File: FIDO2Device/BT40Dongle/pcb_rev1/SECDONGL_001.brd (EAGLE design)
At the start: 24 x 34 mm, 38 parts, among them CN1 CX60-24S-UNIT, CN2 IF_5PIN_H, CN3 IF_2PIN_SOL, SW1 SKRPACE010, SW2 SKRPACE010, SW3 SKTADAE010, U1 BT40, U2 ADP122ACPZ-3.3-R7, U3 RV-3028-C7

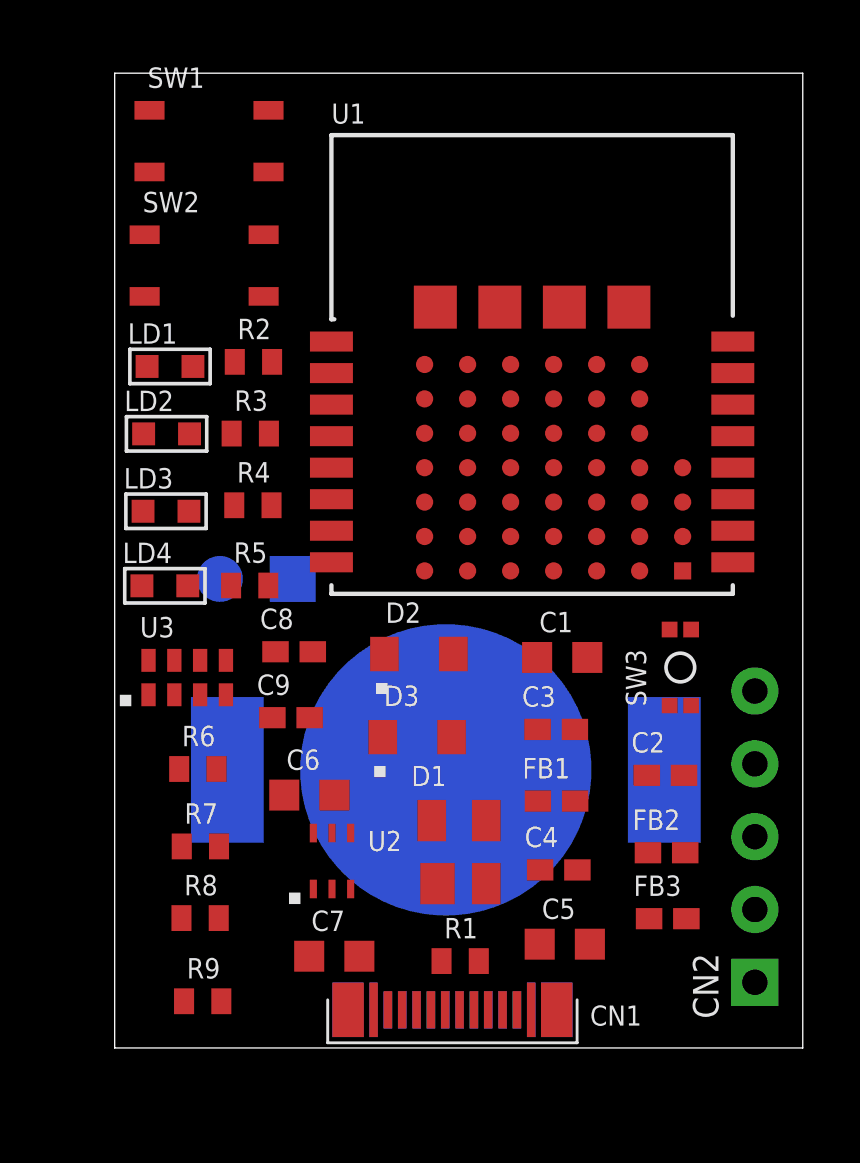
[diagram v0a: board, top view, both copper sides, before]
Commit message: 配線レイアウトを作成
・部品のおおまかなレイアウトを設定
・チップ抵抗のパッケージから、Keepoutを削除
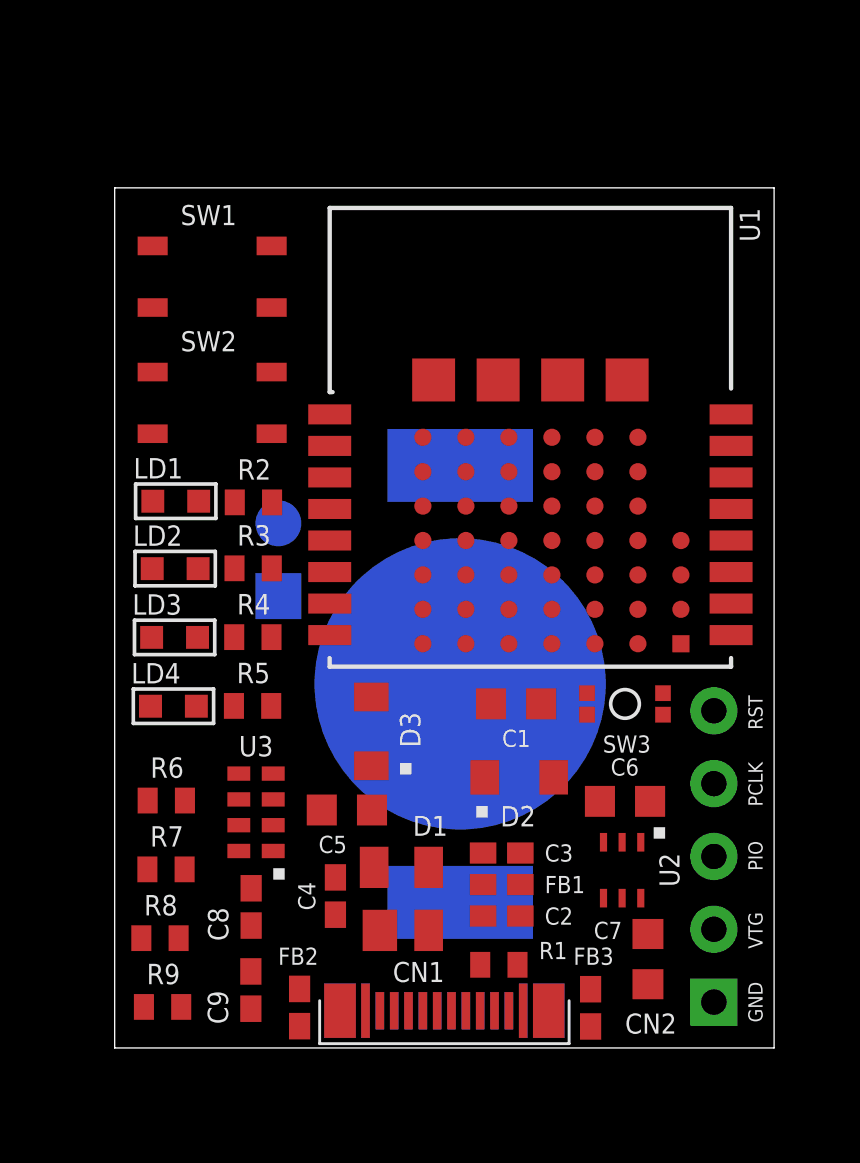
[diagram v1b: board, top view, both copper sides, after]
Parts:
- moved FB2 13.9 mm to (6.45, 1.41), turned to 270 degrees
- moved C6 11.0 mm to (17.8, 8.60), turned to 180 degrees
- moved C7 10.9 mm to (18.6, 3.10), turned to 270 degrees
- moved U2 10.1 mm to (17.7, 6.20), turned to 180 degrees
- moved C9 9.60 mm to (4.75, 2.02), turned to 90 degrees
- moved C8 9.03 mm to (4.76, 4.92), turned to 90 degrees
- moved C5 8.93 mm to (8.10, 8.30), turned to 180 degrees
- moved C4 7.84 mm to (7.70, 5.30), turned to 270 degrees
- moved C2 7.53 mm to (13.5, 4.60)
- moved U3 7.29 mm to (5.93, 6.62), turned to 90 degrees
- moved D2 5.54 mm to (14.1, 9.44)
- moved R2 4.90 mm to (4.84, 19.0)
- moved SW2 4.80 mm to (3.40, 22.5)
- moved SW1 4.73 mm to (3.40, 26.9)
- moved C3 4.71 mm to (13.5, 6.80)
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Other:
- board size 24 x 34 mm -> 23 x 30 mm
- board text added: "GND"
- board text added: "PCLK"
- board text added: "PIO"
- board text added: "RST"
- board text added: "VTG"

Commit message: 配線レイアウトの作成
・サイズを小型化（30mm x 20mm）するため、部品レイアウトを修正
・部品番号を変更（FBx --> Lx）
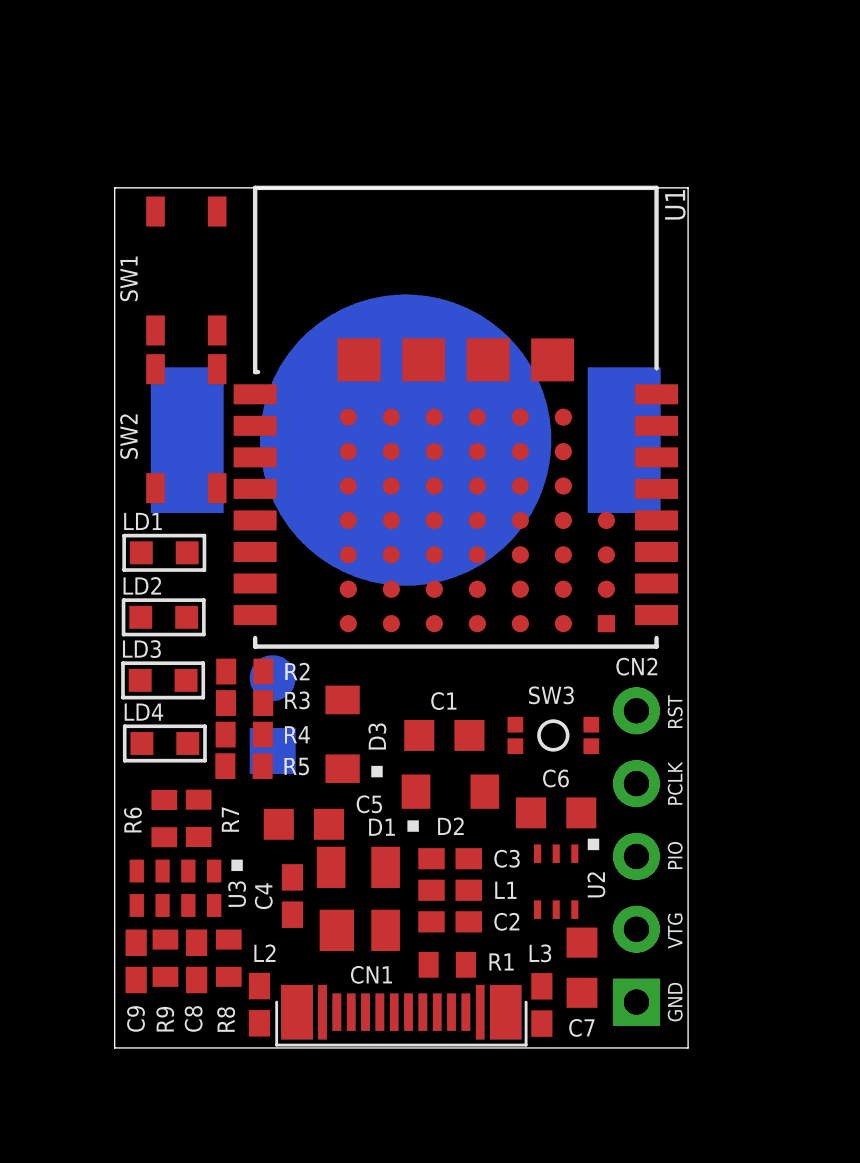
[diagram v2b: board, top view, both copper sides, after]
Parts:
- removed FB1, FB2, FB3: BLM15AG121SN1D, Parts:C0402K
- added L1, L2, L3: BLM15AG121SN1D, Parts:C0402K
- moved BAT1 8.71 mm to (10.2, 21.2), turned to 180 degrees
- moved R2 5.91 mm to (4.54, 13.1)
- moved CN3 5.40 mm to (5.51, 10.4)
- moved R3 4.71 mm to (4.53, 12.0)
- moved C9 4.12 mm to (0.75, 3.02), turned to 270 degrees
- moved R4 3.41 mm to (4.52, 10.9)
- moved C1 2.73 mm to (11.5, 10.9), turned to 0 degrees
- moved SW3 2.73 mm to (15.3, 10.9)
- moved CN2 2.70 mm to (18.2, 1.60)
- moved U1 2.69 mm to (4.90, 14.0)
- moved C8 2.69 mm to (2.86, 3.02), turned to 270 degrees
- moved R8 2.50 mm to (3.98, 3.13), turned to 90 degrees
- moved D2 2.45 mm to (11.7, 8.94)
- moved C6 2.43 mm to (15.4, 8.20)
- moved U2 2.33 mm to (15.4, 5.80)
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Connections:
- net 0V: now also L2.2, L3.2; no longer FB2.2, FB3.2
- net FG: now also L3.1; no longer FB3.1
- net USB_GND: now also L2.1; no longer FB2.1
- net VBUS: now also L1.1; no longer FB1.1
- net VBUS_NRF: now also L1.2; no longer FB1.2
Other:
- board size 23 x 30 mm -> 20 x 30 mm

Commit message: 配線レイアウトを作成
・部品位置を修正
・centroidを試し出し
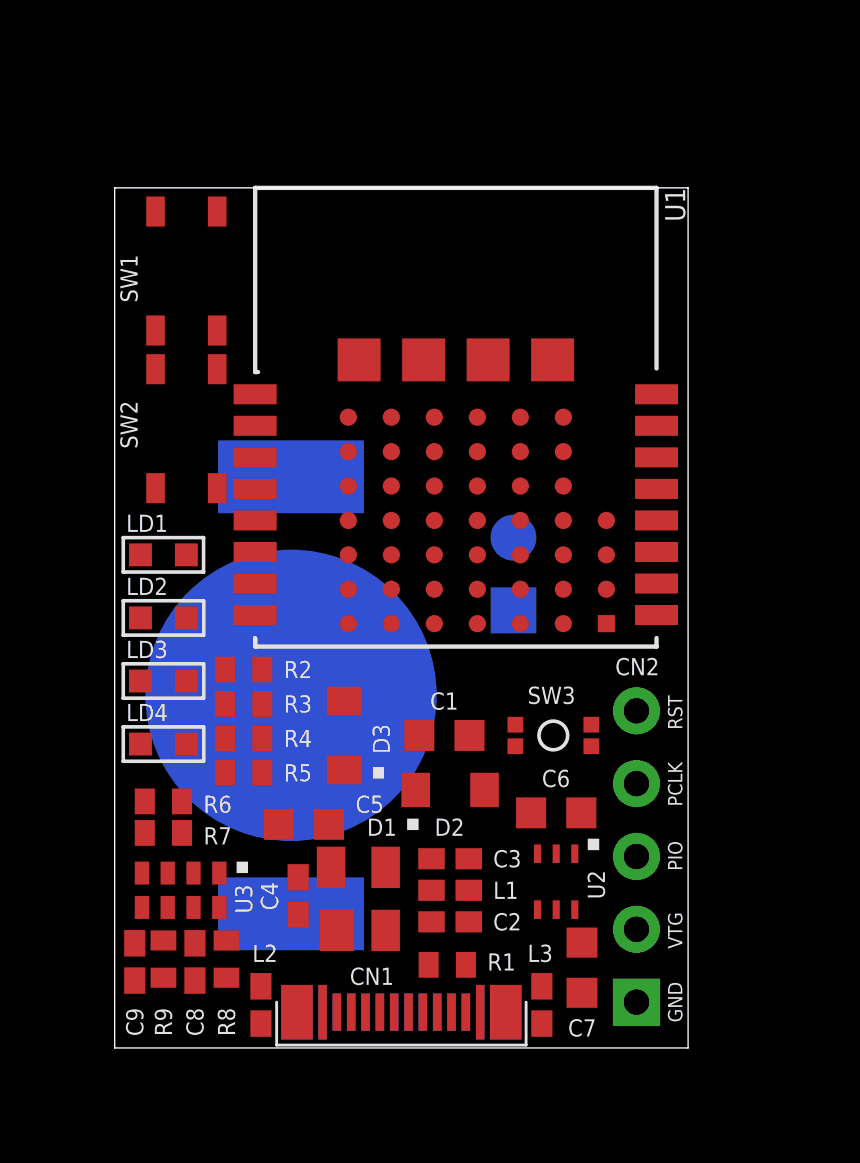
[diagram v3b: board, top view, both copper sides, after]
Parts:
- moved BAT1 9.76 mm to (6.15, 12.3), turned to 90 degrees
- moved CN3 9.72 mm to (13.9, 15.3)
- moved R7 1.33 mm to (1.70, 7.50), turned to 180 degrees
- moved R6 0.60 mm to (1.70, 8.60), turned to 180 degrees
- moved R5 0.23 mm to (4.50, 9.60), turned to 180 degrees
- moved C4 0.20 mm to (6.40, 5.30)
- moved U3 0.19 mm to (3.90, 6.50)
- moved R4 0.13 mm to (4.50, 10.8), turned to 180 degrees
- moved R8 0.09 mm to (3.90, 3.10)
- moved R2 0.08 mm to (4.50, 13.2), turned to 180 degrees
- moved LD1 0.08 mm to (1.70, 17.2)
- moved R9 0.08 mm to (1.70, 3.10)
- moved D3 0.06 mm to (8.00, 10.9)
- moved C8 0.06 mm to (2.80, 3.00)
- moved D2 0.06 mm to (11.7, 9.00)
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
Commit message: 配線レイアウトを作成
・USBコネクター周りの配線
・Viaの穴径は0.3mmで統一しています。
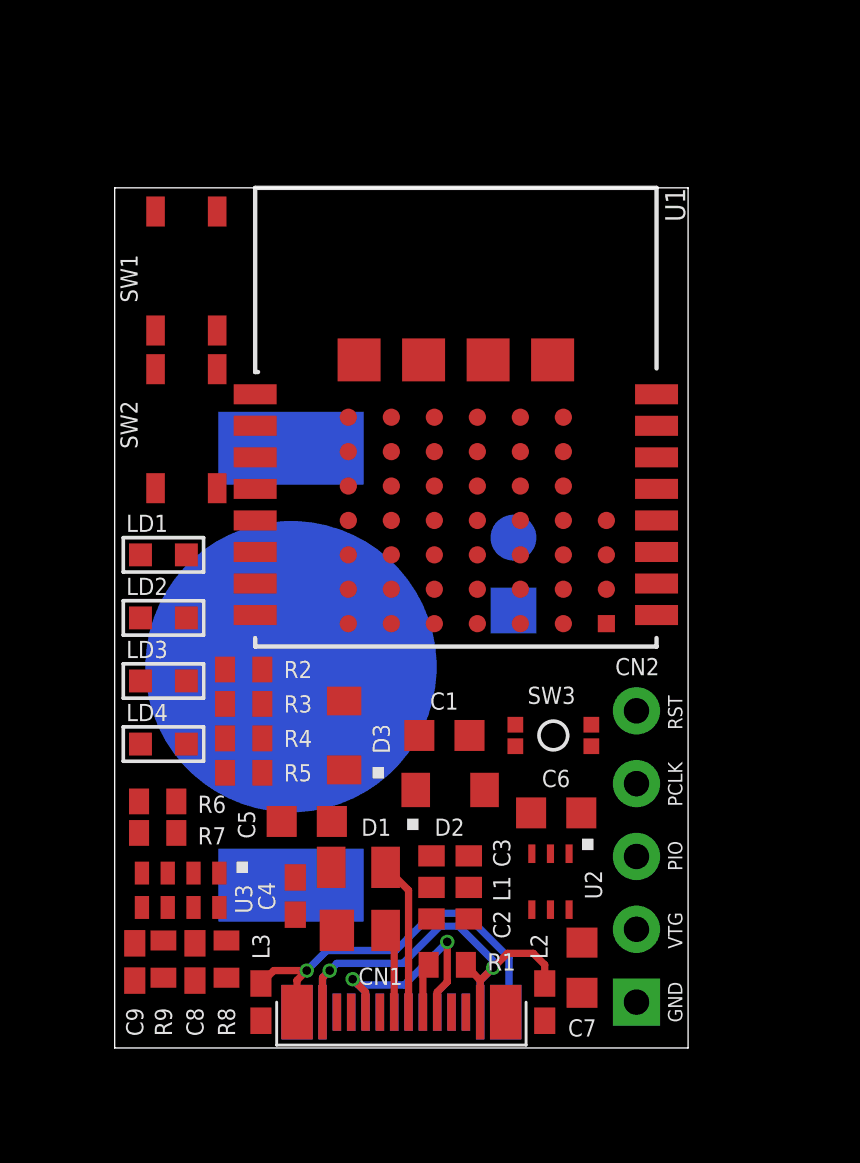
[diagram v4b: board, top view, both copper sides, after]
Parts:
- moved L2 9.90 mm to (15.0, 1.60)
- moved L3 9.80 mm to (5.10, 1.60)
- moved BAT1 1.00 mm to (6.15, 13.3)
- moved U2 0.20 mm to (15.2, 5.80)
- moved R6 0.20 mm to (1.50, 8.60)
- moved R7 0.20 mm to (1.50, 7.50)
- moved C5 0.14 mm to (6.70, 7.90)
- moved C3 0.10 mm to (11.7, 6.70)
- moved C4 0.10 mm to (6.30, 5.30)
- moved C2 0.10 mm to (11.7, 4.50)
- moved L1 0.10 mm to (11.7, 5.60)
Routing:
- net USB_GND: track 0.00 -> 17.2 mm, vias 0 -> 2
- net FG: track 0.00 -> 13.8 mm, vias 0 -> 1
- net VBUS: track 0.00 -> 11.9 mm, vias 0 -> 2
- net D_P: track 0.00 -> 5.38 mm
- net D_N: track 0.00 -> 2.97 mm
- net N$2: track 0.00 -> 1.73 mm

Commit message: 配線レイアウトを作成
・USB差動信号、SWD／RESET信号を配線
（２面目を使用）
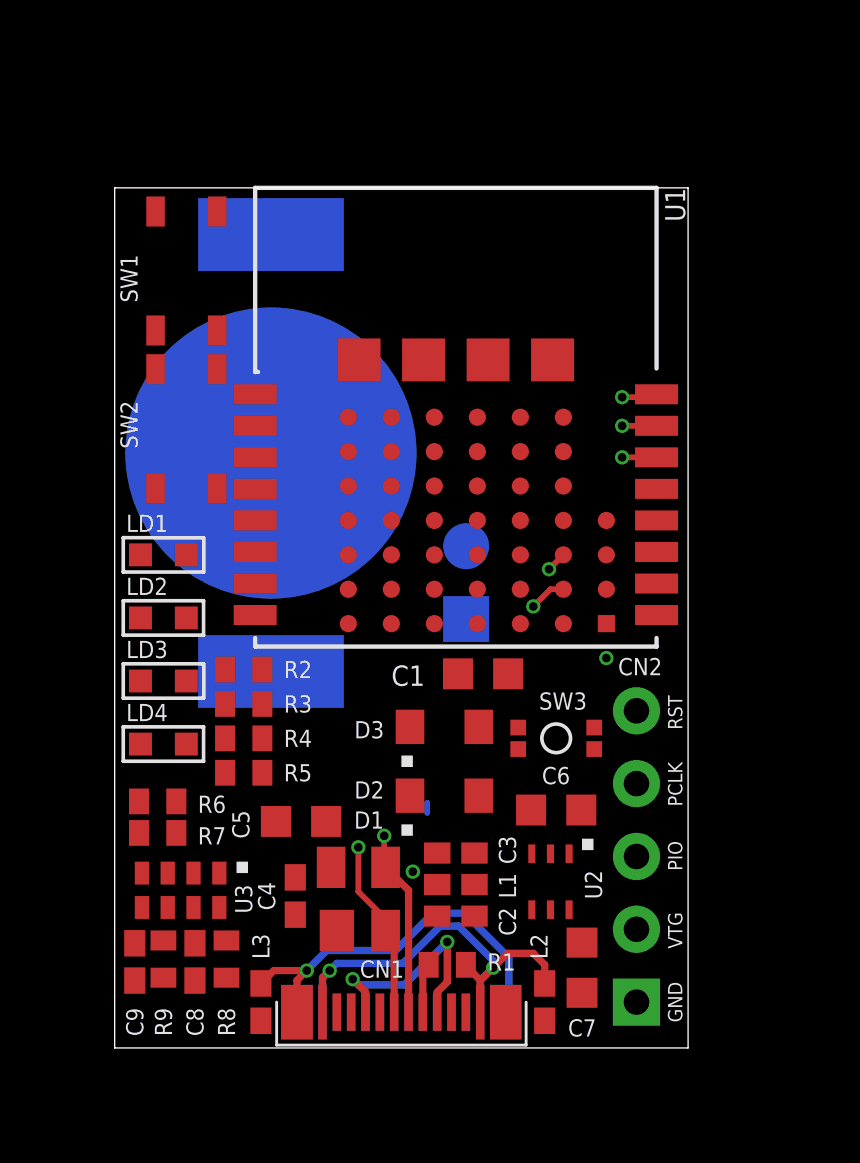
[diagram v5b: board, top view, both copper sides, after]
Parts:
- moved BAT1 7.48 mm to (5.45, 20.8)
- moved D3 3.51 mm to (11.5, 11.2), turned to 0 degrees
- moved C1 2.54 mm to (12.8, 13.1)
- moved CN3 1.68 mm to (12.3, 15.0)
- moved D2 0.28 mm to (11.5, 8.80)
- moved L1 0.22 mm to (11.9, 5.70)
- moved C2 0.22 mm to (11.9, 4.60)
- moved C3 0.22 mm to (11.9, 6.80)
- moved C5 0.20 mm to (6.50, 7.90)
- moved SW3 0.14 mm to (15.4, 10.8)
- moved C6 0.10 mm to (15.4, 8.30)
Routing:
- net SWDIO: track 0.00 -> 19.1 mm, vias 0 -> 1
- net D_N: track 2.97 -> 18.5 mm, vias 0 -> 2
- net SWCLK: track 0.00 -> 15.2 mm, vias 0 -> 1
- net D_P: track 5.38 -> 19.1 mm, vias 0 -> 2
- net RESET: track 0.00 -> 11.2 mm, vias 0 -> 1
- net VBUS_NRF: track 0.00 -> 0.35 mm, vias 0 -> 1
- net VBUS: vias 2 -> 3
